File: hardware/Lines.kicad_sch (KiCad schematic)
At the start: 28 parts, among them K10 L4_COIN_CTRL, K3 L1_HOLD, K4 L1_COIN_CTRL, K5 L2_HOLD, K6 L2_COIN_CTRL, K7 L3_HOLD, K8 L3_COIN_CTRL, K9 L4_HOLD, U10 ILD74, U7 ILD74, U8 ILD74, U9 ILD74

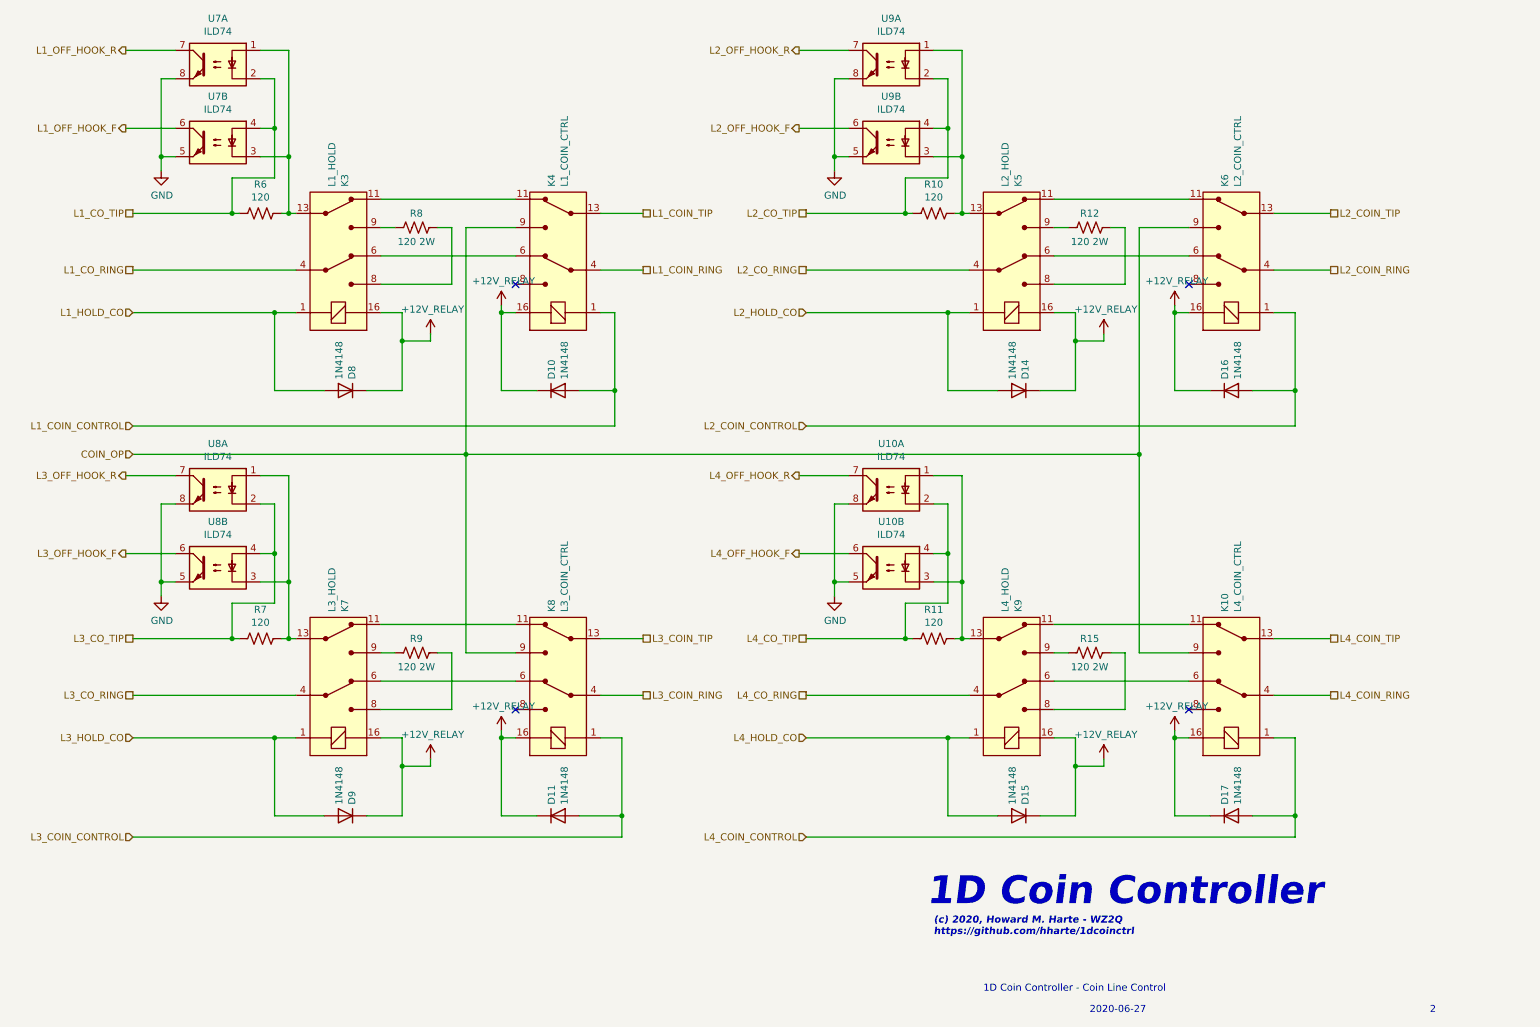
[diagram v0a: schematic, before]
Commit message: Issue 3:
* Remove barrel jack, replace with 4-position terminal block with
  provision for +/- 130VDC input in case the user already has an
  appropriate power supply and does not want the on-board
  DC-DC converter.  Note: 130V DC-DC converter PS2, relay
  K8, C14, D10, and R16 must be omitted during assembly.
* Add bi-color LEDs for line status.
  Green=Off-hook, normal polarity.
  Red=Off-hook, reverse polarity.
  Off=on-hook.
* Add header for FTDI USB UART, if user does not RS-232 UART levels.
  To use the FTDI header, do not populate U1 and other components on
  pp. 3 of the schematic.
* Remove i2c I/O expander and use PIC GPIOs directly.
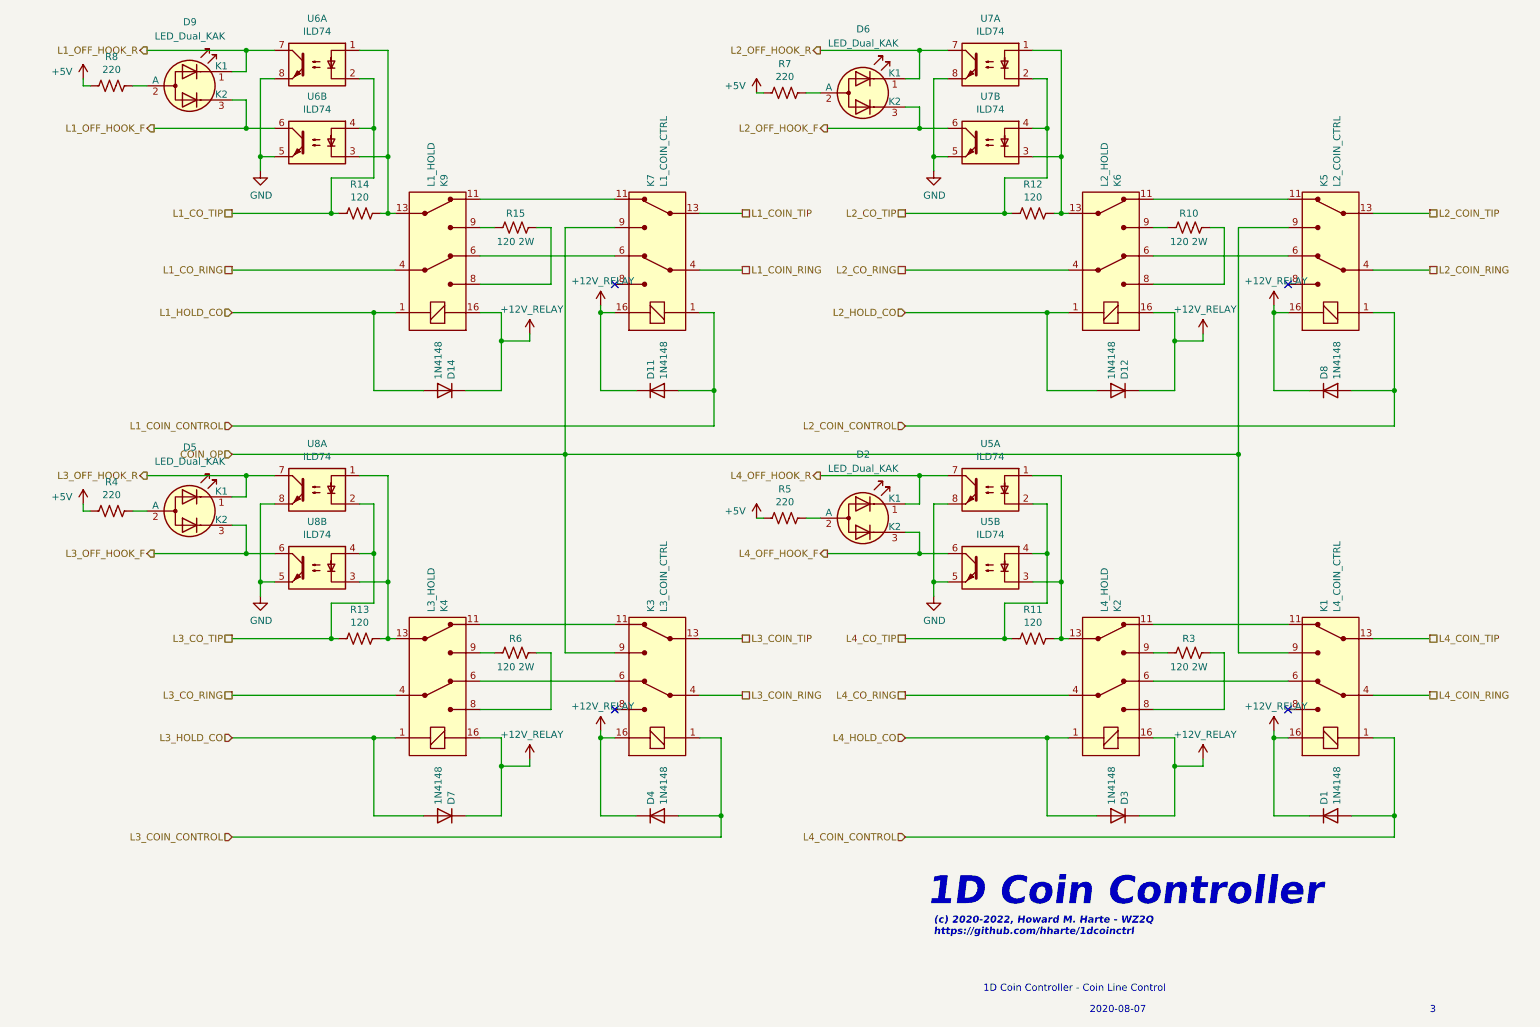
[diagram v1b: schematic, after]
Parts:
- added D2, D5, D6, D9: LED_Dual_KAK, LED_THT:LED_D5.0mm-3, symbol Device:LED_Dual_KAK
- added R4, R5, R7, R8: 220, Resistor_THT:R_Axial_DIN0207_L6.3mm_D2.5mm_P7.62mm_Horizontal, symbol Device:R_US
- K1: renamed from K10; Digi-Key_PN Z768-ND -> PB1125-ND
- K2: renamed from K9; Digi-Key_PN Z768-ND -> PB1125-ND
- K3: renamed from K8; Digi-Key_PN Z768-ND -> PB1125-ND
- K4: renamed from K7; Digi-Key_PN Z768-ND -> PB1125-ND
- K5: renamed from K6; Digi-Key_PN Z768-ND -> PB1125-ND
- K6: renamed from K5; Digi-Key_PN Z768-ND -> PB1125-ND
- K7: renamed from K4; Digi-Key_PN Z768-ND -> PB1125-ND
- K9: renamed from K3; Digi-Key_PN Z768-ND -> PB1125-ND
- renumbered D17 to D1, D10 to D11, D14 to D12, D8 to D14, D15 to D3, D11 to D4, D9 to D7, D16 to D8, R12 to R10, R10 to R12, R7 to R13, R6 to R14, R8 to R15, R15 to R3, R9 to R6, U10 to U5, U7 to U6, U9 to U7
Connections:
- net L1_OFF_HOOK_F: now also D9.3 (K2)
- net L1_OFF_HOOK_R: now also D9.1 (K1)
- net L2_OFF_HOOK_F: now also D6.3 (K2)
- net L2_OFF_HOOK_R: now also D6.1 (K1)
- net L3_OFF_HOOK_F: now also D5.3 (K2)
- net L3_OFF_HOOK_R: now also D5.1 (K1)
- net L4_OFF_HOOK_F: now also D2.3 (K2)
- net L4_OFF_HOOK_R: now also D2.1 (K1)
- new net: D5.2 (A), R4.1
- new net: D9.2 (A), R8.1
- new net: D2.2 (A), R5.1
- new net: D6.2 (A), R7.1
- new net +5V: R4.2, R5.2, R7.2, R8.2
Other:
- note added: "(c) 2020-2022, Howard M. Harte - WZ2Q https://github.com/hharte/1dcoinctrl"
- note added: "2020-08-07"
- note added: "3"
- note removed: "(c) 2020, Howard M. Harte - WZ2Q https://github.com/hharte/1dcoinctrl"
- note removed: "2"
- note removed: "2020-06-27"
- moved on the sheet: D1, D11, D12, D14, D3, D4, D7, D8, K1, K2, K3, K4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

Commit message: Issue 4: Switch from PIC to AVR128DA28 MCU.
    * The AVR128DA28 is supported by the Arduino IDE.
    * Simpler UPDI programming.
    * Update to KiCAD 8.0.1
    * Fix footprint outline for IA1224S DC-DC converter.
    * Add initial Arduino firmware for AVR128DA28 MCU.
    * Move Earth Ground hole.
    * Add jumpers for UART and UPDI configuration.
    * Add 3D-printable end caps for Hammond enclosure.
    * Geographical reannotate PCB.
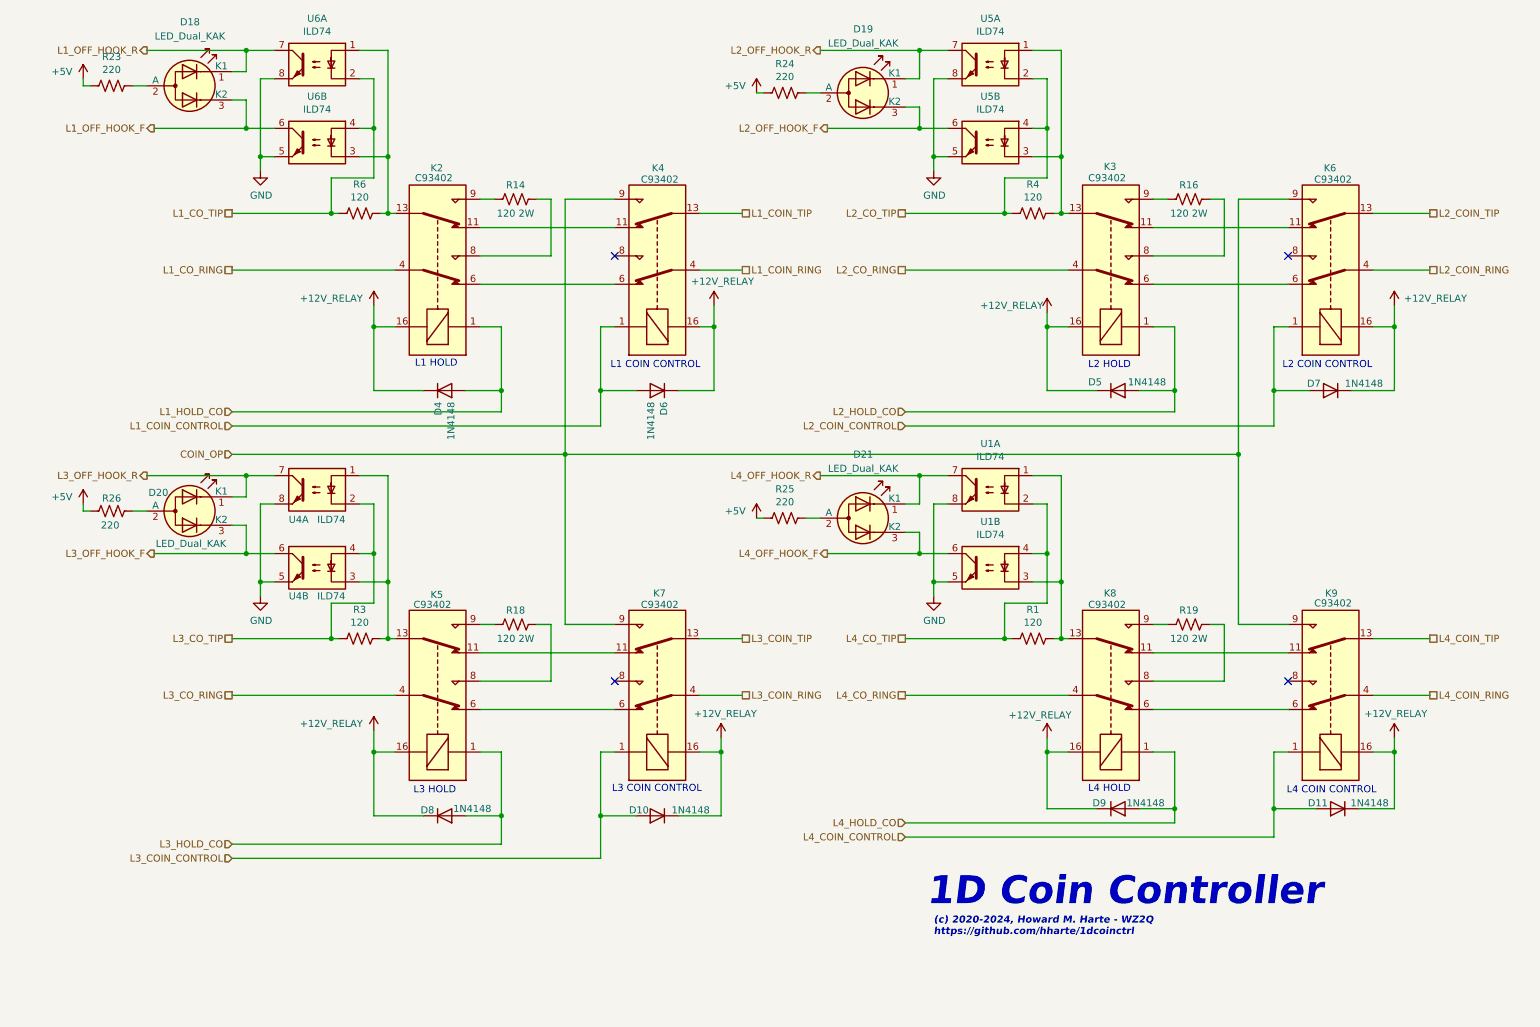
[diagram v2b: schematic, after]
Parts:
- removed R15: 120 2W, Resistor_THT:R_Axial_DIN0516_L15.5mm_D5.0mm_P20.32mm_Horizontal, symbol Device:R_US
- added R14: 120 2W, Resistor_THT:R_Axial_DIN0516_L15.5mm_D5.0mm_P20.32mm_Horizontal, symbol Device:R_US
- D10: renamed from D4; Digi-Key_PN (none) -> 1N4148TACT-ND; MPN (none) -> 1N4148TA
- D11: renamed from D1; Digi-Key_PN (none) -> 1N4148TACT-ND; MPN (none) -> 1N4148TA
- D18: renamed from D9; Digi-Key_PN (none) -> 1497-1357-ND; MPN (none) -> XLMDKVG59MCA
- D19: renamed from D6; Digi-Key_PN (none) -> 1497-1357-ND; MPN (none) -> XLMDKVG59MCA
- D20: renamed from D5; Digi-Key_PN (none) -> 1497-1357-ND; MPN (none) -> XLMDKVG59MCA
- D21: renamed from D2; Digi-Key_PN (none) -> 1497-1357-ND; MPN (none) -> XLMDKVG59MCA
- D4: renamed from D14; Digi-Key_PN (none) -> 1N4148TACT-ND; MPN (none) -> 1N4148TA
- D5: renamed from D12; Digi-Key_PN (none) -> 1N4148TACT-ND; MPN (none) -> 1N4148TA
- D6: renamed from D11; Digi-Key_PN (none) -> 1N4148TACT-ND; MPN (none) -> 1N4148TA
- D7: renamed from D8; Digi-Key_PN (none) -> 1N4148TACT-ND; MPN (none) -> 1N4148TA
- D8: renamed from D7; Digi-Key_PN (none) -> 1N4148TACT-ND; MPN (none) -> 1N4148TA
- D9: renamed from D3; Digi-Key_PN (none) -> 1N4148TACT-ND; MPN (none) -> 1N4148TA
- K2: renamed from K9; value L1_HOLD -> C93402; footprint digikey-footprints:Relay_THT_G5V-2 -> Relay_THT:Relay_DPDT_Omron_G5V-2; symbol 1d_coinctrl_r2-rescue:G5V-2-DC12-dk_Signal-Relays-Up-to-2-Amps -> Relay:G5V-2; DK_Datasheet_Link http://omronfs.omron.com/en_US/ecb/products/pdf/en-g5v_2.pdf -> https://omronfs.omron.com/en_US/ecb/products/pdf/en-g5v_2.p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; MPN G5V-2-DC12 -> C93402
- K3: renamed from K6; value L2_HOLD -> C93402; footprint digikey-footprints:Relay_THT_G5V-2 -> Relay_THT:Relay_DPDT_Omron_G5V-2; symbol 1d_coinctrl_r2-rescue:G5V-2-DC12-dk_Signal-Relays-Up-to-2-Amps -> Relay:G5V-2; DK_Datasheet_Link http://omronfs.omron.com/en_US/ecb/products/pdf/en-g5v_2.pdf -> https://omronfs.omron.com/en_US/ecb/products/pdf/en-g5v_2.p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; MPN G5V-2-DC12 -> C93402
- K4: renamed from K7; value L1_COIN_CTRL -> C93402; footprint digikey-footprints:Relay_THT_G5V-2 -> Relay_THT:Relay_DPDT_Omron_G5V-2; symbol 1d_coinctrl_r2-rescue:G5V-2-DC12-dk_Signal-Relays-Up-to-2-Amps -> Relay:G5V-2; DK_Datasheet_Link http://omronfs.omron.com/en_US/ecb/products/pdf/en-g5v_2.pdf -> https://omronfs.omron.com/en_US/ecb/products/pdf/en-g5v_2.p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; MPN G5V-2-DC12 -> C93402
- K5: renamed from K4; value L3_HOLD -> C93402; footprint digikey-footprints:Relay_THT_G5V-2 -> Relay_THT:Relay_DPDT_Omron_G5V-2; symbol 1d_coinctrl_r2-rescue:G5V-2-DC12-dk_Signal-Relays-Up-to-2-Amps -> Relay:G5V-2; DK_Datasheet_Link http://omronfs.omron.com/en_US/ecb/products/pdf/en-g5v_2.pdf -> https://omronfs.omron.com/en_US/ecb/products/pdf/en-g5v_2.p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; MPN G5V-2-DC12 -> C93402
- K6: renamed from K5; value L2_COIN_CTRL -> C93402; footprint digikey-footprints:Relay_THT_G5V-2 -> Relay_THT:Relay_DPDT_Omron_G5V-2; symbol 1d_coinctrl_r2-rescue:G5V-2-DC12-dk_Signal-Relays-Up-to-2-Amps -> Relay:G5V-2; DK_Datasheet_Link http://omronfs.omron.com/en_US/ecb/products/pdf/en-g5v_2.pdf -> https://omronfs.omron.com/en_US/ecb/products/pdf/en-g5v_2.p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; MPN G5V-2-DC12 -> C93402
- K7: renamed from K3; value L3_COIN_CTRL -> C93402; footprint digikey-footprints:Relay_THT_G5V-2 -> Relay_THT:Relay_DPDT_Omron_G5V-2; symbol 1d_coinctrl_r2-rescue:G5V-2-DC12-dk_Signal-Relays-Up-to-2-Amps -> Relay:G5V-2; DK_Datasheet_Link http://omronfs.omron.com/en_US/ecb/products/pdf/en-g5v_2.pdf -> https://omronfs.omron.com/en_US/ecb/products/pdf/en-g5v_2.p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; MPN G5V-2-DC12 -> C93402
- K8: renamed from K2; value L4_HOLD -> C93402; footprint digikey-footprints:Relay_THT_G5V-2 -> Relay_THT:Relay_DPDT_Omron_G5V-2; symbol 1d_coinctrl_r2-rescue:G5V-2-DC12-dk_Signal-Relays-Up-to-2-Amps -> Relay:G5V-2; DK_Datasheet_Link http://omronfs.omron.com/en_US/ecb/products/pdf/en-g5v_2.pdf -> https://omronfs.omron.com/en_US/ecb/products/pdf/en-g5v_2.p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; MPN G5V-2-DC12 -> C93402
- K9: renamed from K1; value L4_COIN_CTRL -> C93402; footprint digikey-footprints:Relay_THT_G5V-2 -> Relay_THT:Relay_DPDT_Omron_G5V-2; symbol 1d_coinctrl_r2-rescue:G5V-2-DC12-dk_Signal-Relays-Up-to-2-Amps -> Relay:G5V-2; DK_Datasheet_Link http://omronfs.omron.com/en_US/ecb/products/pdf/en-g5v_2.pdf -> https://omronfs.omron.com/en_US/ecb/products/pdf/en-g5v_2.p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; MPN G5V-2-DC12 -> C93402
- R1: renamed from R11; Digi-Key_PN (none) -> S120HCT-ND; MPN (none) -> CFM12JT120R
- R16: renamed from R10; Digi-Key_PN (none) -> 120ZCT-ND; MPN (none) -> FMP200JR-52-120R
- R18: renamed from R6; Digi-Key_PN (none) -> 120ZCT-ND; MPN (none) -> FMP200JR-52-120R
- R19: renamed from R3; Digi-Key_PN (none) -> 120ZCT-ND; MPN (none) -> FMP200JR-52-120R
- R23: renamed from R8; Digi-Key_PN (none) -> S220HCT-ND; MPN (none) -> CFM12JT220R
- R24: renamed from R7; Digi-Key_PN (none) -> S220HCT-ND; MPN (none) -> CFM12JT220R
- R25: renamed from R5; Digi-Key_PN (none) -> S220HCT-ND; MPN (none) -> CFM12JT220R
- R26: renamed from R4; Digi-Key_PN (none) -> S220HCT-ND; MPN (none) -> CFM12JT220R
- R3: renamed from R13; Digi-Key_PN (none) -> S120HCT-ND; MPN (none) -> CFM12JT120R
- R4: renamed from R12; Digi-Key_PN (none) -> S120HCT-ND; MPN (none) -> CFM12JT120R
- R6: renamed from R14; Digi-Key_PN (none) -> S120HCT-ND; MPN (none) -> CFM12JT120R
- U1: renamed from U5; Digi-Key_PN (none) -> CNY74-2H-ND; MPN (none) -> CNY74-2H
- U4: renamed from U8; Digi-Key_PN (none) -> CNY74-2H-ND; MPN (none) -> CNY74-2H
- U5: renamed from U7; Digi-Key_PN (none) -> CNY74-2H-ND; MPN (none) -> CNY74-2H
- U6: Digi-Key_PN (none) -> CNY74-2H-ND; MPN (none) -> CNY74-2H
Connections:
- net at K2.8: now also R14.1
- net at K2.9: now also R14.2
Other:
- note added: "(c) 2020-2024, Howard M. Harte - WZ2Q https://github.com/hharte/1dcoinctrl"
- note added: "L1 COIN CONTROL"
- note added: "L1 HOLD"
- note added: "L2 COIN CONTROL"
- note added: "L2 HOLD"
- note added: "L3 COIN CONTROL"
- note added: "L3 HOLD"
- note added: "L4 COIN CONTROL"
- note added: "L4 HOLD"
- note removed: "(c) 2020-2022, Howard M. Harte - WZ2Q https://github.com/hharte/1dcoinctrl"
- note removed: "1D Coin Controller - Coin Line Control"
- note removed: "2020-08-07"
- note removed: "3"
- title: (none) -> 1D Coin Controller - Coin Line Control
- moved on the sheet: D10, D11, D6, D7, D9, R16, R18, R19
